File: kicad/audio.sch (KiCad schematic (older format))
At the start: 14 parts, among them J10 PC_AUDIO_EXTRA, J11 Jack header, J12 Jack header, J13 L/R channel choice, J14 Jack header, J15 CITA/OMTP choice, J16 TRRS/TRS+TS choice, J17 Audio header, J18 Xcvr grounding jumpers, J19 XCVR_Audio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

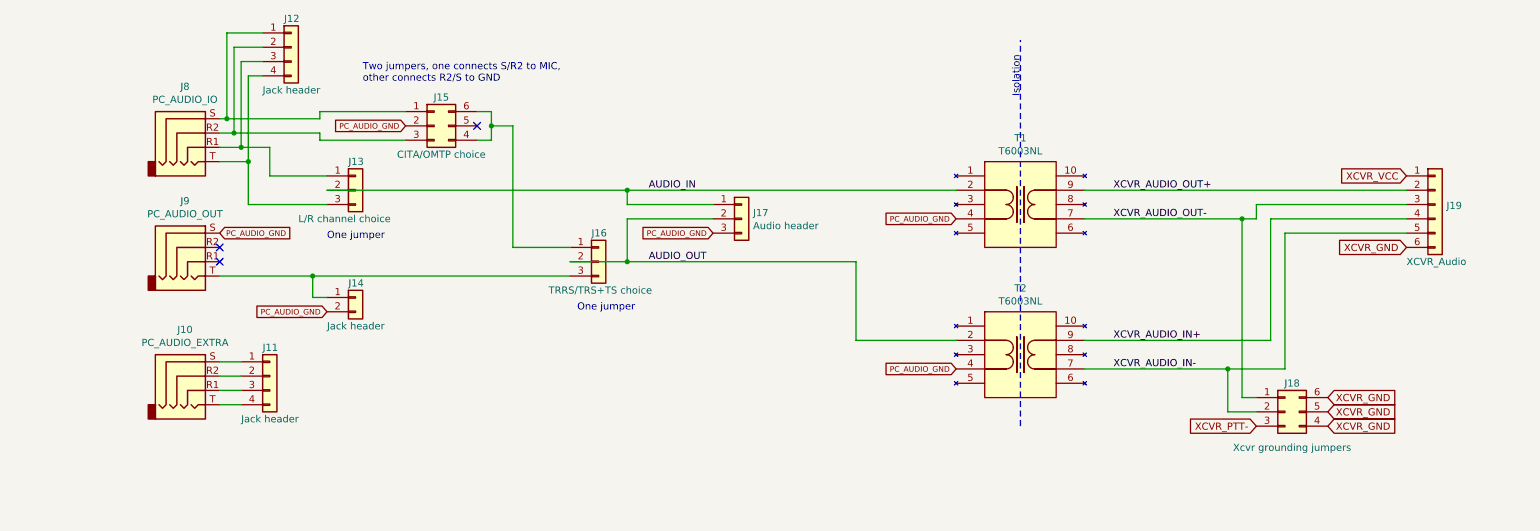
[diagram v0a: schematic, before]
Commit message: Filtering, jumpers, LEDs, misc
* Modified high level diagram to express the shared UART bus
* Renamed XCVR_VCC to XCVR_13V8
* Add solder jumpers on audio, PTT and UART lines for easy prototyping/bypassing
* Added bypass caps on XCVR side data and audio connectors
* Add series ferite beads on data ICs Vcc
* Added schottky diodes to all XCVR_13V8
* Changed series resistors of RXLED/TXLED/VccLED for 6mA current
* Added power LEDs on XCVR_13V8 connector terminals
* Added power LED for XCVR_5V rail
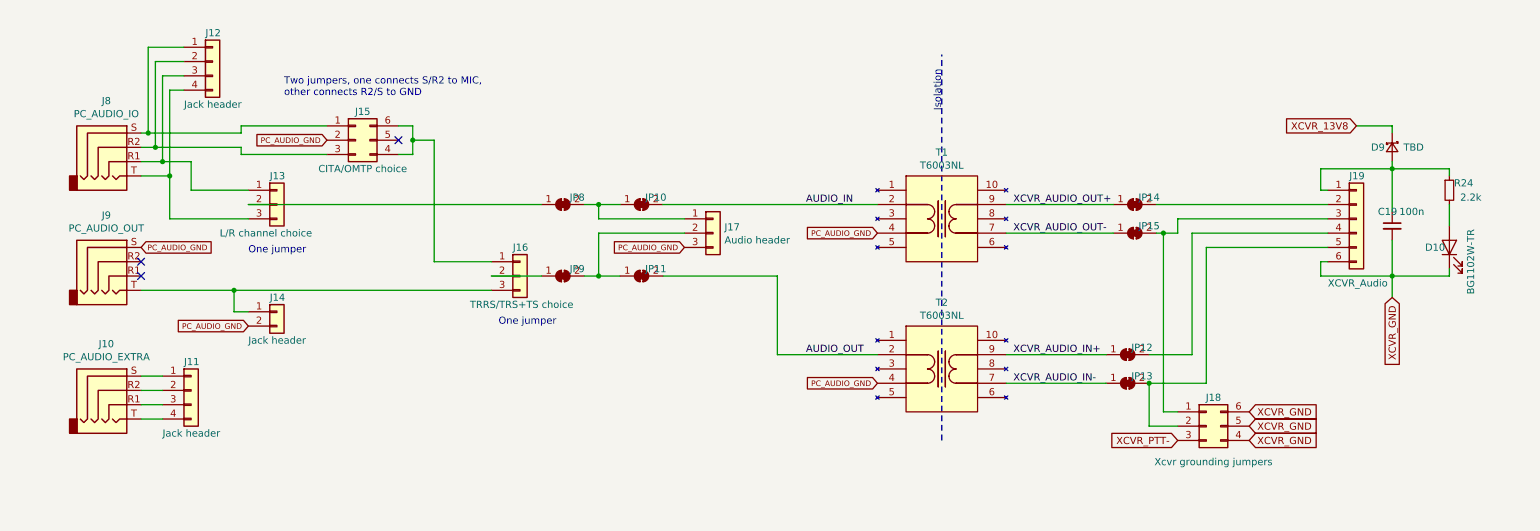
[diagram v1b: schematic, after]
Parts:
- added C19: 100n, symbol Device:C_Small
- added D10: BG1102W-TR, symbol Device:LED
- added D9: TBD, symbol Device:D_Schottky_Small
- added JP10, JP11, JP12, JP13, JP14, JP15, JP8, JP9: SolderJumper_2_Bridged, symbol Jumper:SolderJumper_2_Bridged
- added R24: 2.2k, symbol Device:R_Small
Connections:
- net AUDIO_IN: now also JP10.2 (B); no longer J13.2 (Pin_2), J17.1 (Pin_1)
- net AUDIO_OUT: now also JP11.2 (B); no longer J16.2 (Pin_2), J17.2 (Pin_2)
- net XCVR_AUDIO_IN+: now also JP12.1 (A); no longer J19.4 (Pin_4)
- net XCVR_AUDIO_IN-: now also JP13.1 (A); no longer J18.2 (Pin_2), J19.5 (Pin_5)
- net XCVR_AUDIO_OUT+: now also JP14.1 (A); no longer J19.2 (Pin_2)
- net XCVR_AUDIO_OUT-: now also JP15.1 (A); no longer J18.1 (Pin_1), J19.3 (Pin_3)
- net XCVR_GND: now also C19.2, D10.1 (K)
- net XCVR_VCC: no longer names the net of J19.1 (Pin_1)
- net XCVR_VCC: now also C19.1, D9.2 (A), R24.1
- new net: J13.2 (Pin_2), JP8.1 (A)
- new net: J16.2 (Pin_2), JP9.1 (A)
- new net: J19.2 (Pin_2), JP14.2 (B)
- new net: J18.1 (Pin_1), J19.3 (Pin_3), JP15.2 (B)
- new net: J19.4 (Pin_4), JP12.2 (B)
- new net: J18.2 (Pin_2), J19.5 (Pin_5), JP13.2 (B)
- new net: J17.1 (Pin_1), JP10.1 (A), JP8.2 (B)
- new net: J17.2 (Pin_2), JP11.1 (A), JP9.2 (B)
- new net: D10.2 (A), R24.2
- new net XCVR_13V8: D9.1 (K)
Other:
- moved on the sheet: J10, J11, J12, J13, J14, J15, J16, J17, J18, J19, J8, J9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

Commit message: MAX driver protection
* Adjust label position for readability
* Protected R1OUT-R3OUT of MAX driver with OR gate
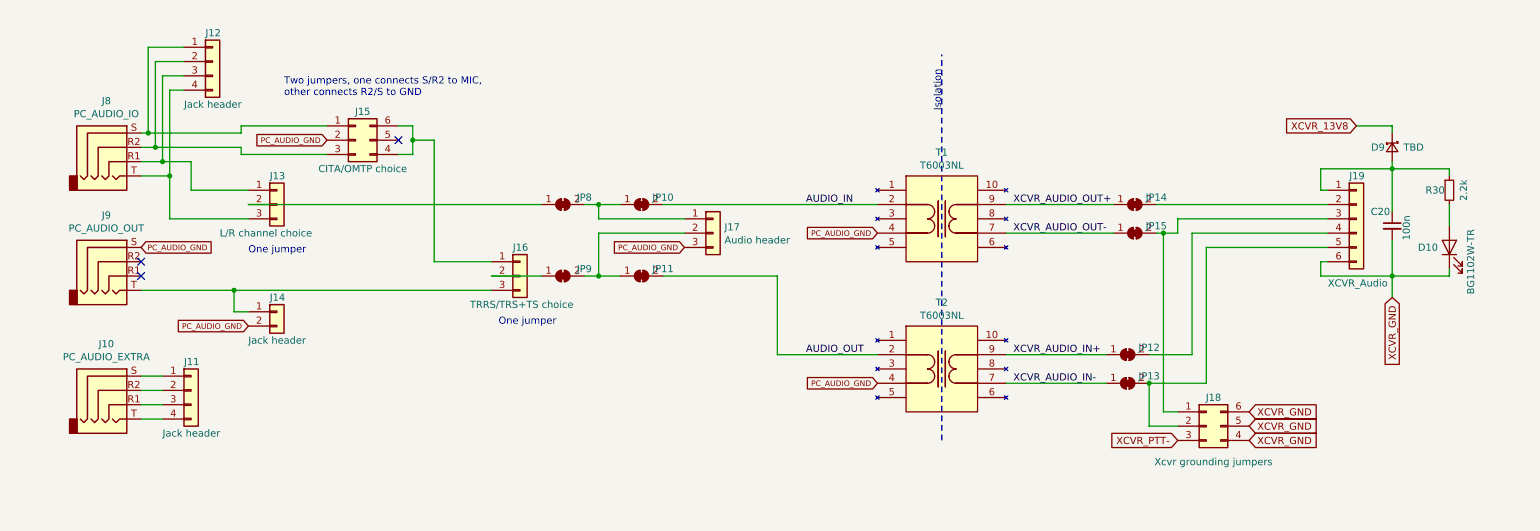
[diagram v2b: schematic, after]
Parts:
- renumbered C19 to C20, R24 to R30
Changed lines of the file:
@@
 $Descr A4 11693 8268
 encoding utf-8
-Sheet 4 4
+Sheet 5 5
 Title "cat-a-hack"
 Date ""
-Rev "r1"
+Rev "r2"
 Comp "Vasile Vilvoiu (YO7JBP)"
 Comment1 "CAT and audio hackable isolation board"
@@
 XCVR_13V8
 $Comp
-L Device:C_Small C19
+L Device:C_Small C20
 U 1 1 5FC37879
 P 10250 3400
-AR Path="/5F9E817D/5FC37879" Ref="C19"  Part="1"
+AR Path="/5F9E817D/5FC37879" Ref="C20"  Part="1"
 AR Path="/5F9E7705/5FC37879" Ref="C?"  Part="1"
-F 0 "C19" H 10150 3500 50  0000 L CNN
-F 1 "100n" H 10300 3500 50  0000 L CNN
+F 0 "C20" H 10100 3500 50  0000 L CNN
+F 1 "100n" V 10350 3300 50  0000 L CNN
 F 2 "" H 10250 3400 50  0001 C CNN
 F 3 "~" H 10250 3400 50  0001 C CNN
@@
 AR Path="/5F9D7A3C/5FDABC92" Ref="R?"  Part="1"
 AR Path="/5F9E7705/5FDABC92" Ref="R?"  Part="1"
-AR Path="/5F9E817D/5FDABC92" Ref="R24"  Part="1"
-F 0 "R24" H 10750 3200 50  0000 C CNN
-F 1 "2.2k" H 10800 3100 50  0000 C CNN
+AR Path="/5F9E817D/5FDABC92" Ref="R30"  Part="1"
+F 0 "R30" H 10550 3150 50  0000 C CNN
+F 1 "2.2k" V 10750 3150 50  0000 C CNN
 F 2 "" H 10650 3150 50  0001 C CNN
 F 3 "~" H 10650 3150 50  0001 C CNN
@@
 AR Path="/5F9E7705/5FDABC98" Ref="D?"  Part="1"
 AR Path="/5F9E817D/5FDABC98" Ref="D10"  Part="1"
-F 0 "D10" V 10650 3650 50  0000 C CNN
+F 0 "D10" V 10650 3700 50  0000 C CNN
 F 1 "BG1102W-TR" H 10550 3400 50  0000 C CNN
 F 2 "" H 10650 3550 50  0001 C CNN
@@
 AR Path="/5F9E7705/5FF738C4" Ref="JP?"  Part="1"
 AR Path="/5F9E817D/5FF738C4" Ref="JP14"  Part="1"
-F 0 "JP14" H 8550 3300 50  0000 C CNN
+F 0 "JP14" H 8600 3300 50  0000 C CNN
 F 1 "SolderJumper_2_Bridged" H 8450 3364 50  0001 C CNN
 F 2 "" H 8450 3250 50  0001 C CNN
@@
 AR Path="/5F9E7705/5FF7A2F0" Ref="JP?"  Part="1"
 AR Path="/5F9E817D/5FF7A2F0" Ref="JP15"  Part="1"
-F 0 "JP15" H 8550 3500 50  0000 C CNN
+F 0 "JP15" H 8600 3500 50  0000 C CNN
 F 1 "SolderJumper_2_Bridged" H 8450 3564 50  0001 C CNN
 F 2 "" H 8450 3450 50  0001 C CNN
@@
 AR Path="/5F9E7705/5FF7BC41" Ref="JP?"  Part="1"
 AR Path="/5F9E817D/5FF7BC41" Ref="JP13"  Part="1"
-F 0 "JP13" H 8500 4550 50  0000 C CNN
+F 0 "JP13" H 8550 4550 50  0000 C CNN
 F 1 "SolderJumper_2_Bridged" H 8400 4614 50  0001 C CNN
 F 2 "" H 8400 4500 50  0001 C CNN
@@
 AR Path="/5F9E7705/5FF7B162" Ref="JP?"  Part="1"
 AR Path="/5F9E817D/5FF7B162" Ref="JP12"  Part="1"
-F 0 "JP12" H 8500 4350 50  0000 C CNN
+F 0 "JP12" H 8550 4350 50  0000 C CNN
 F 1 "SolderJumper_2_Bridged" H 8400 4414 50  0001 C CNN
 F 2 "" H 8400 4300 50  0001 C CNN
@@
 AR Path="/5F9E7705/5FF7DD37" Ref="JP?"  Part="1"
 AR Path="/5F9E817D/5FF7DD37" Ref="JP10"  Part="1"
-F 0 "JP10" H 5100 3300 50  0000 C CNN
+F 0 "JP10" H 5150 3300 50  0000 C CNN
 F 1 "SolderJumper_2_Bridged" H 5000 3364 50  0001 C CNN
 F 2 "" H 5000 3250 50  0001 C CNN
@@
 AR Path="/5F9E7705/5FF7F2F6" Ref="JP?"  Part="1"
 AR Path="/5F9E817D/5FF7F2F6" Ref="JP8"  Part="1"
-F 0 "JP8" H 4550 3300 50  0000 C CNN
+F 0 "JP8" H 4600 3300 50  0000 C CNN
 F 1 "SolderJumper_2_Bridged" H 4450 3364 50  0001 C CNN
 F 2 "" H 4450 3250 50  0001 C CNN
@@
 AR Path="/5F9E7705/5FF8015D" Ref="JP?"  Part="1"
 AR Path="/5F9E817D/5FF8015D" Ref="JP11"  Part="1"
-F 0 "JP11" H 5100 3800 50  0000 C CNN
+F 0 "JP11" H 5150 3800 50  0000 C CNN
 F 1 "SolderJumper_2_Bridged" H 5000 3864 50  0001 C CNN
 F 2 "" H 5000 3750 50  0001 C CNN
@@
 AR Path="/5F9E7705/5FF7F79F" Ref="JP?"  Part="1"
 AR Path="/5F9E817D/5FF7F79F" Ref="JP9"  Part="1"
-F 0 "JP9" H 4550 3800 50  0000 C CNN
+F 0 "JP9" H 4600 3800 50  0000 C CNN
 F 1 "SolderJumper_2_Bridged" H 4450 3864 50  0001 C CNN
 F 2 "" H 4450 3750 50  0001 C CNN

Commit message: Initial footprint placement + changes
* Added initial placement
* Remove pull-down resistors from USB lines.
* Remove ferrite bead from FTDI chip as it was very close to Vcc FB
* Fixed MAX TX pins
* Assigned footprints.
* Removed redundant solder jumpers.
* Small changes for layout coherence.
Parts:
- removed J15: CITA/OMTP choice, symbol Connector_Generic:Conn_02x03_Counter_Clockwise
- removed J18: Xcvr grounding jumpers, symbol Connector_Generic:Conn_02x03_Counter_Clockwise
- removed JP10, JP11, JP8, JP9: SolderJumper_2_Bridged, symbol Jumper:SolderJumper_2_Bridged
- added J15: CITA/OMTP choice, Connector_PinHeader_2.54mm:PinHeader_2x03_P2.54mm_Vertical, symbol Connector_Generic:Conn_02x03_Odd_Even
- added J18: Xcvr grounding jumpers, Connector_PinHeader_2.54mm:PinHeader_2x03_P2.54mm_Vertical, symbol Connector_Generic:Conn_02x03_Odd_Even
- C20: footprint (none) -> Capacitor_SMD:C_1206_3216Metric_Pad1.42x1.75mm_HandSolder
- D10: footprint (none) -> LED_SMD:LED_1206_3216Metric_Pad1.42x1.75mm_HandSolder
- D9: value TBD -> 1N4148X-TP; footprint (none) -> Diode_SMD:D_SOD-523
- J10, J8, J9: footprint (none) -> custom:SJ43514
- J11, J12: footprint (none) -> Connector_PinHeader_2.54mm:PinHeader_1x04_P2.54mm_Vertical
- J13, J16, J17: footprint (none) -> Connector_PinHeader_2.54mm:PinHeader_1x03_P2.54mm_Vertical
- J14: footprint (none) -> Connector_PinHeader_2.54mm:PinHeader_1x02_P2.54mm_Vertical
- J19: footprint (none) -> custom:TB003-500-P06BE
- JP12, JP13, JP14, JP15: footprint (none) -> Jumper:SolderJumper-2_P1.3mm_Bridged_RoundedPad1.0x1.5mm
- R30: footprint (none) -> Resistor_SMD:R_1206_3216Metric_Pad1.42x1.75mm_HandSolder
- T1, T2: footprint T6003NL -> custom:T6003NL_HandSolder
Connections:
- net AUDIO_IN: now also J13.2 (Pin_2), J17.1 (Pin_1)
- net AUDIO_OUT: now also J16.2 (Pin_2), J17.2 (Pin_2)
- net PC_AUDIO_GND: now also J14.1 (Pin_1), J15.3 (Pin_3); no longer J14.2 (Pin_2)
- net XCVR_GND: now also J18.2 (Pin_2), J18.4 (Pin_4), J18.6 (Pin_6)
- net XCVR_PTT-: now also J18.5 (Pin_5)
- net at J12.1 (Pin_1), J8.S: now also J15.1 (Pin_1)
- net at J12.2 (Pin_2), J8.R2: now also J15.5 (Pin_5)
- net at J16.1 (Pin_1): now also J15.2 (Pin_2), J15.6 (Pin_6)
- net at J16.3 (Pin_3), J9.T: now also J14.2 (Pin_2); no longer J14.1 (Pin_1)
- net at J19.3 (Pin_3), JP15.2 (B): now also J18.1 (Pin_1)
- net at J19.5 (Pin_5), JP13.2 (B): now also J18.3 (Pin_3)
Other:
- moved on the sheet: J14

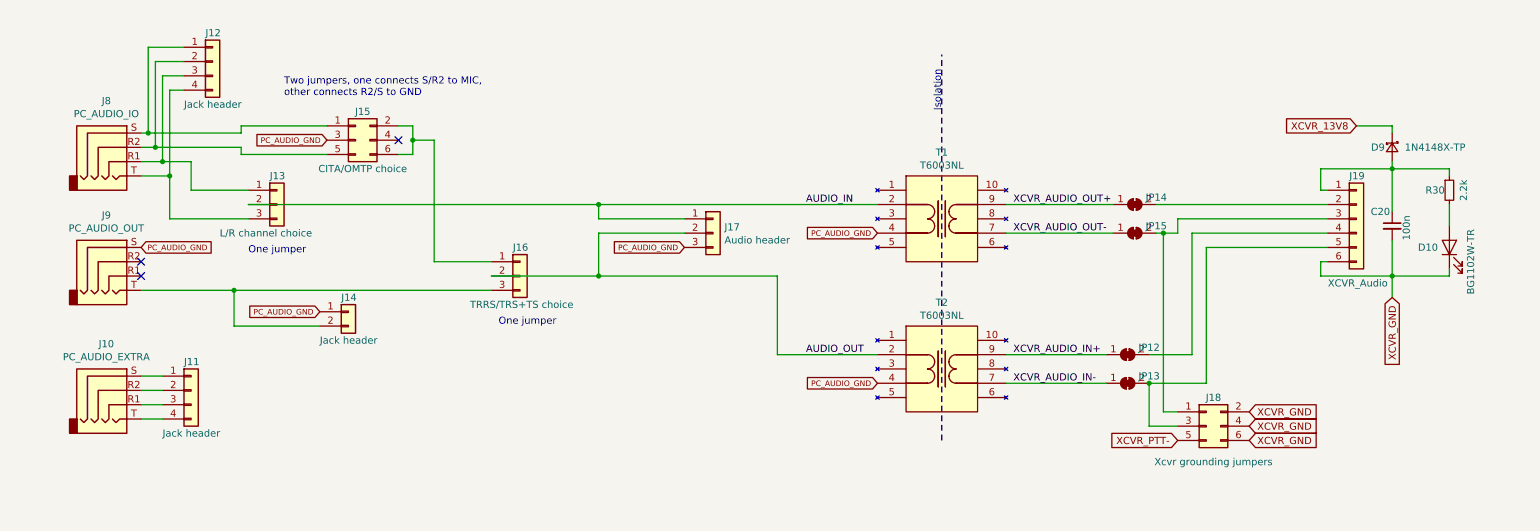
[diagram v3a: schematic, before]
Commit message: New layout, routing, misc...
* Redo layout
* Fixed MAX pulldown resistors on data lines.
* Added jumpers in case MAX not installed.
* Remove audio header
* Remove some redundant solder jumpers
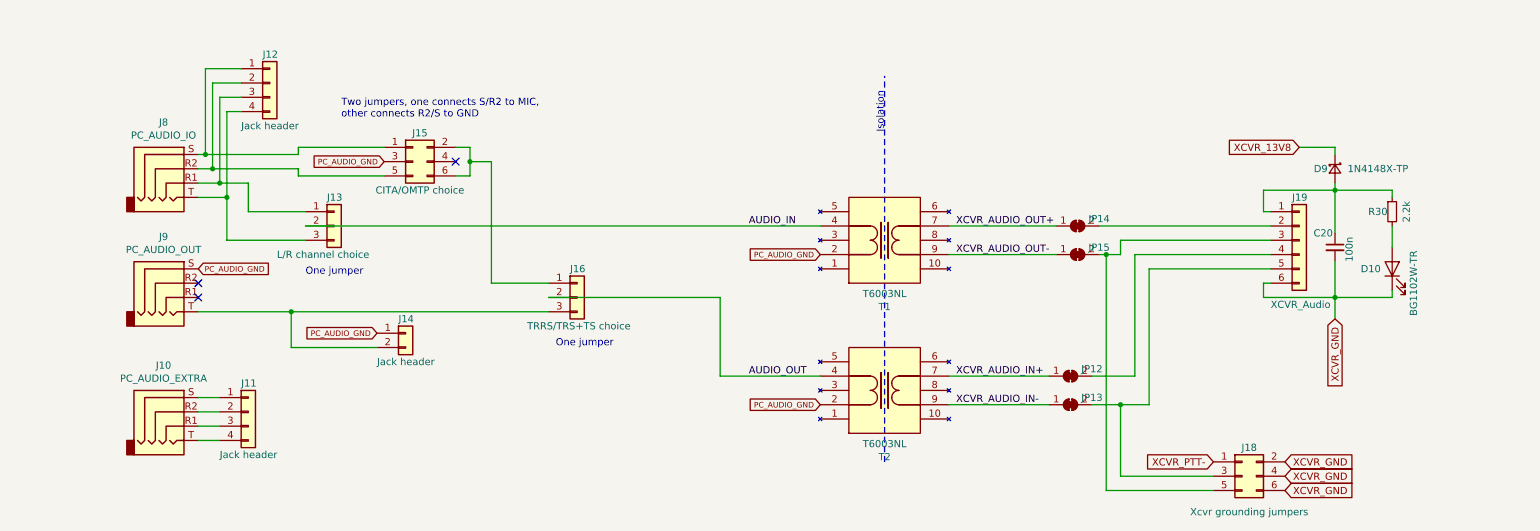
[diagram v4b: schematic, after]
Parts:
- removed J17: Audio header, Connector_PinHeader_2.54mm:PinHeader_1x03_P2.54mm_Vertical, symbol Connector_Generic:Conn_01x03
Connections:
- net AUDIO_IN: now also T1.4; no longer T1.2
- net AUDIO_OUT: now also T2.4; no longer T2.2
- net PC_AUDIO_GND: now also T1.2, T2.2; no longer T1.4, T2.4
- net XCVR_AUDIO_IN+: now also T2.7; no longer T2.9
- net XCVR_AUDIO_IN-: now also T2.9; no longer T2.7
- net XCVR_AUDIO_OUT+: now also T1.7; no longer T1.9
- net XCVR_AUDIO_OUT-: now also T1.9; no longer T1.7
- net XCVR_PTT-: now also J18.1 (Pin_1); no longer J18.5 (Pin_5)
- net at J19.3 (Pin_3), JP15.2 (B): now also J18.5 (Pin_5); no longer J18.1 (Pin_1)
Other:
- moved on the sheet: C20, D10, D9, J10, J11, J12, J13, J14, J15, J16, J18, J19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

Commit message: Audio filtering, hackable area, misc
* Added bypass caps and ferrites to audio lines
* Small rerouting
* Hackable area
* Added rev no
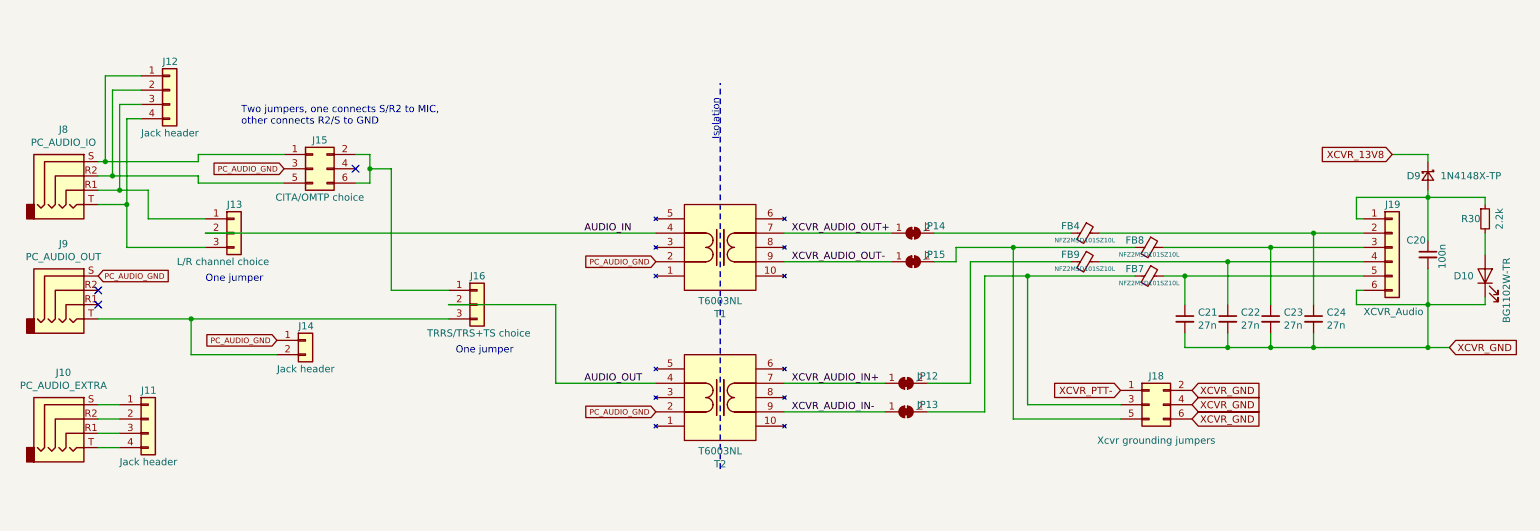
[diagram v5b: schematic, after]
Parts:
- added C21, C22, C23, C24: 27n, Capacitor_SMD:C_1206_3216Metric_Pad1.42x1.75mm_HandSolder, symbol Device:C_Small
- added FB4, FB7, FB8, FB9: NFZ2MSD101SZ10L, custom:NFZ2MSD101SZ10L_0806_Handsolder, symbol Device:Ferrite_Bead_Small
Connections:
- net XCVR_GND: now also C21.2, C22.2, C23.2, C24.2
- net at J19.2 (Pin_2): now also C24.1, FB4.1; no longer JP14.2 (B)
- net at J18.5 (Pin_5), JP15.2 (B): now also FB8.2; no longer J19.3 (Pin_3)
- net at J19.4 (Pin_4): now also C22.1, FB9.1; no longer JP12.2 (B)
- net at J18.3 (Pin_3), JP13.2 (B): now also FB7.2; no longer J19.5 (Pin_5)
- new net: C23.1, FB8.1, J19.3 (Pin_3)
- new net: C21.1, FB7.1, J19.5 (Pin_5)
- new net: FB4.2, JP14.2 (B)
- new net: FB9.2, JP12.2 (B)
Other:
- moved on the sheet: C20, D10, D9, J10, J11, J12, J13, J14, J15, J16, J18, J19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
